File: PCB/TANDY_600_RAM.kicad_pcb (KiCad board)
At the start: 2 copper layers, 68.6 x 45.1 mm, 7 parts, among them J1 DIN 41612 2x22 male right-ang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, U1 628128_SOP, U2 74HC08

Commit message: gnd on tiny, new dual sch, bus connector symbol & footprint
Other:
- board text added: "${COMMENT2} ${REVISION}"
- board text added: "C1,C2: ${00000000-0000-0000-0000-0000587f5e14:VALUE}"
- board text added: "a1"
- board text added: "a22"
- board text added: "b1"
- board text added: "b22"
- board text removed: "${COMMENT2} ${TITLE} v${REVISION}"
- board text removed: "1A"
- board text removed: "1B"
- board text removed: "22A"
- board text removed: "22B"

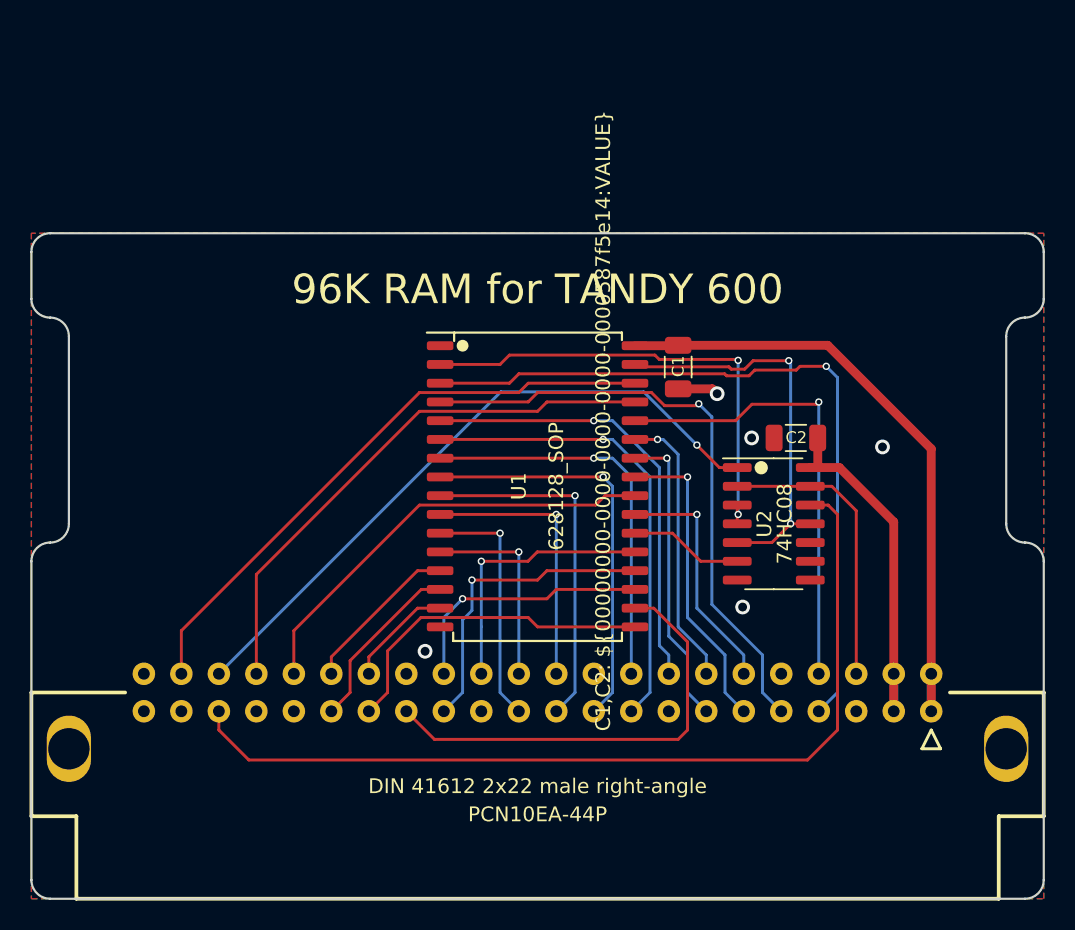
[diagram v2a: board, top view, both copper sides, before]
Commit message: footprints, ground paths
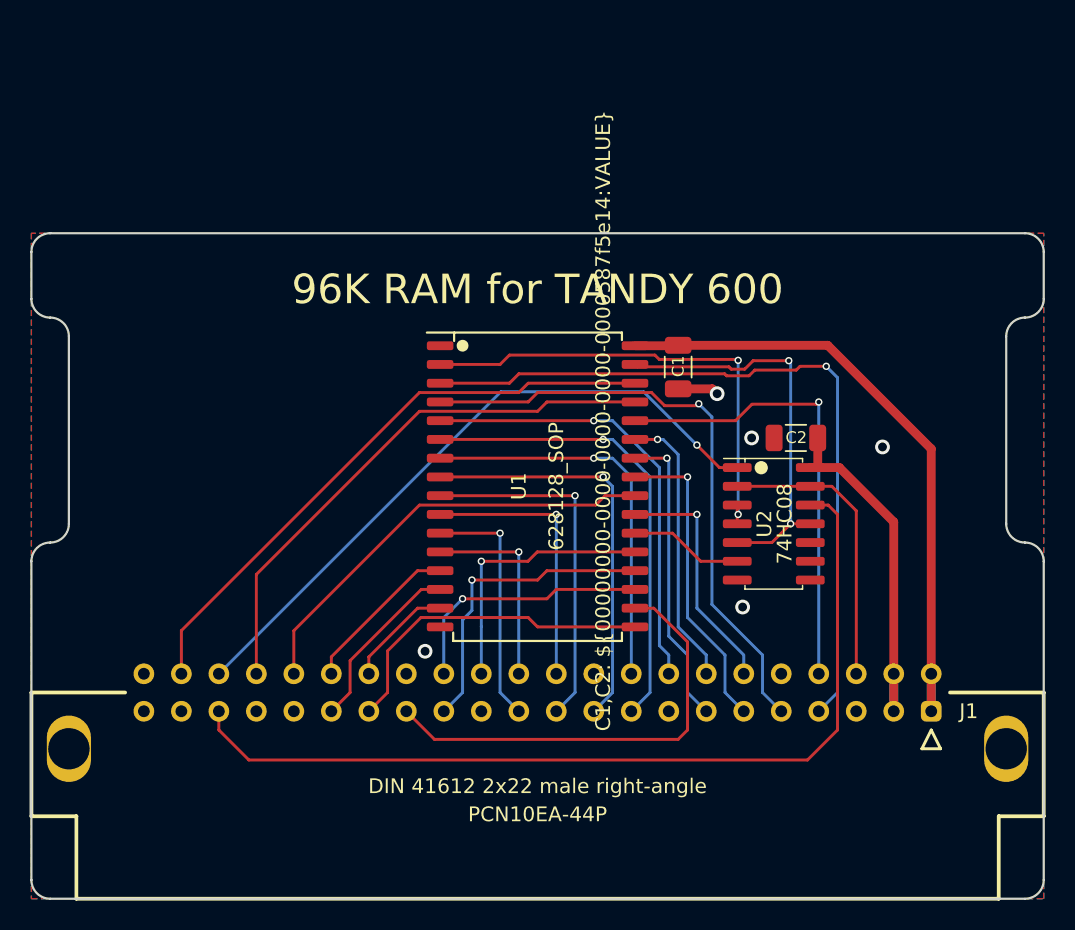
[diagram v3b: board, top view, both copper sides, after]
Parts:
- J1: footprint 000_LOCAL:DIN 41612 2x22 male right-angle -> 000_LOCAL:DIN-41612_02x22_male_horizontal

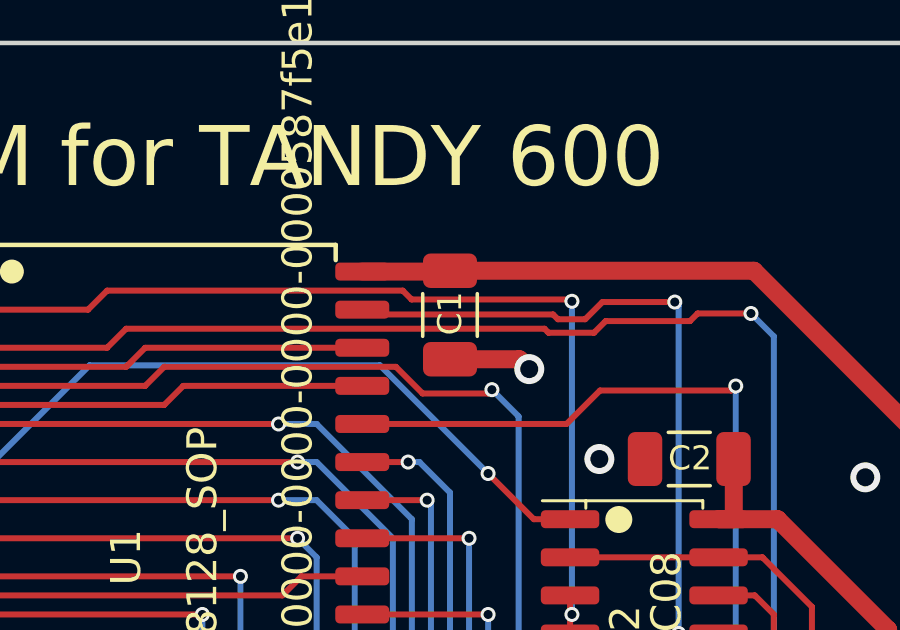
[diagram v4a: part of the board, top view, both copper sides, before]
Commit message: rename 3d dir to 3dshapes to standardize
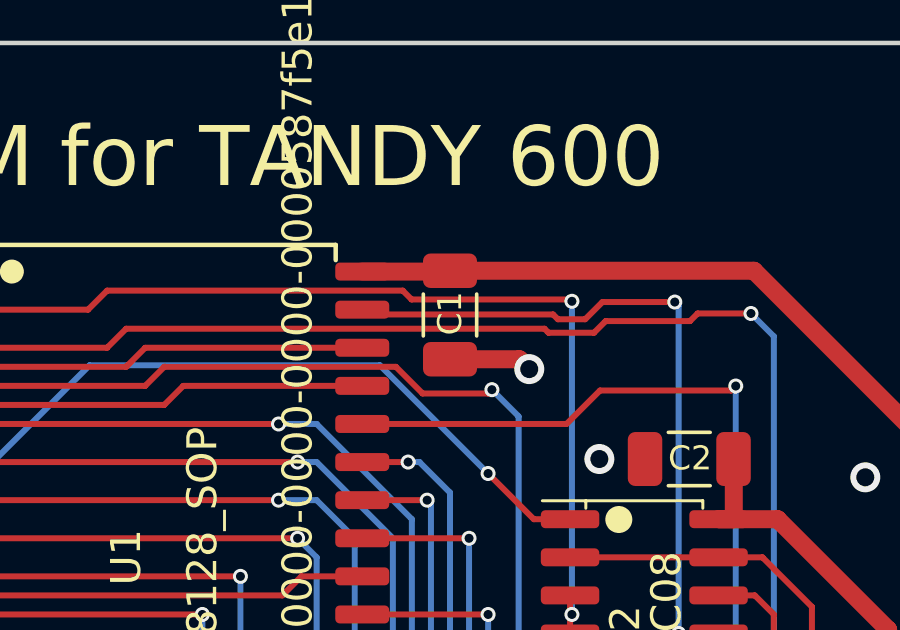
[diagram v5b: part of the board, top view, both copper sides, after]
